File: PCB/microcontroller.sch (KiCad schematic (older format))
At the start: 6 parts, among them U1 DEV_KIT_EK-TM4C123GXL, U301 MC14504B

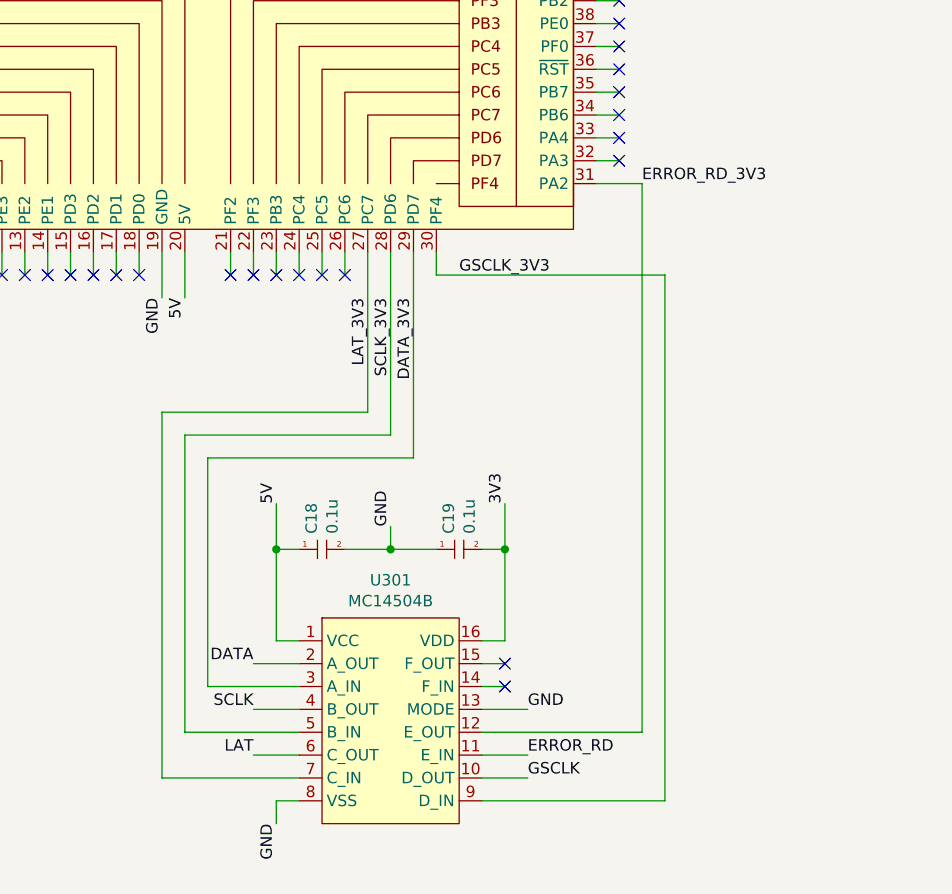
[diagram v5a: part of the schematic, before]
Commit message: V1.0 Ready for Review
Added compatability with the 430BOOST-C55AUDIO1 booster pack.
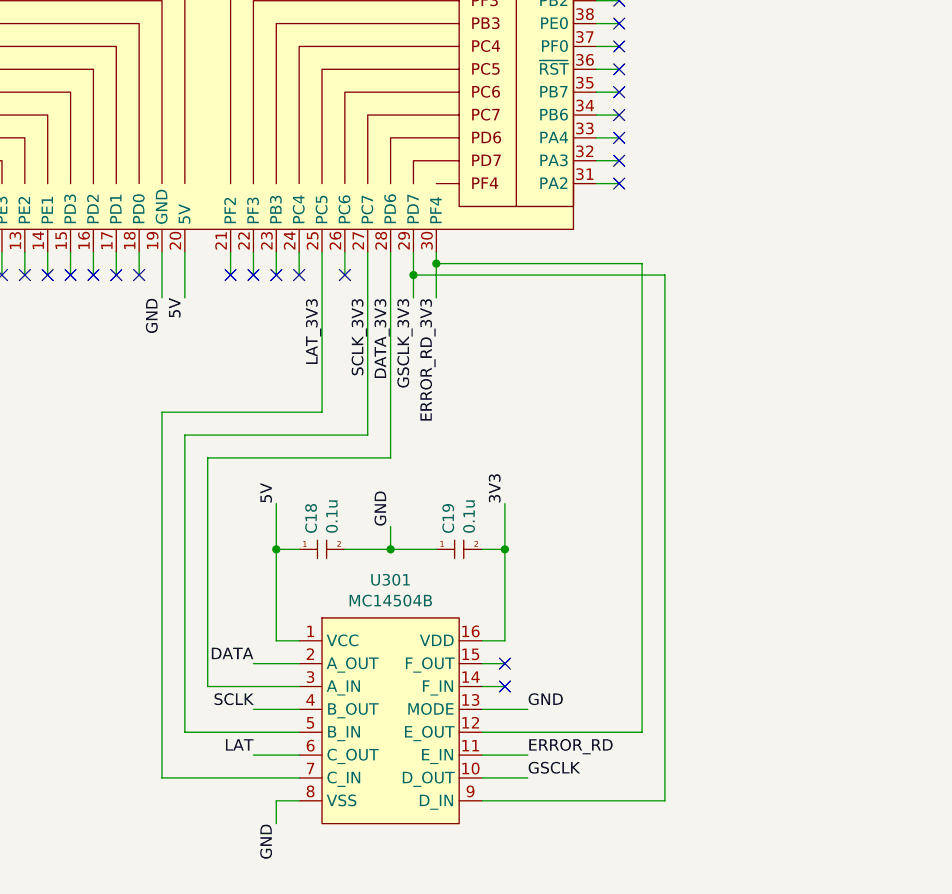
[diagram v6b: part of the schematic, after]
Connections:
- net DATA_3V3: now also U1.28 (PD6); no longer U1.29 (PD7)
- net ERROR_RD_3V3: now also U1.30 (PF4); no longer U1.31 (PA2)
- net GSCLK_3V3: now also U1.29 (PD7); no longer U1.30 (PF4)
- net LAT_3V3: now also U1.25 (PC5); no longer U1.27 (PC7)
- net SCLK_3V3: now also U1.27 (PC7); no longer U1.28 (PD6)
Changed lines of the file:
@@
 Sheet 3 20
 Title "Christmas Tree Disco"
-Date "2017-08-01"
+Date "2017-08-08"
 Rev "01"
 Comp "www.GitHub.com/Cryochasm"
@@
 Wire Wire Line
 	6700 5400 7400 5400
-Wire Wire Line
-	7200 3000 7400 3000
-Wire Wire Line
-	7400 3000 7400 5400
 NoConn ~ 6800 5100
 NoConn ~ 6800 5200
 Wire Wire Line
-	6500 3300 6500 3400
-Wire Wire Line
-	6500 3400 7500 3400
+	6500 3300 6500 3500
 Wire Wire Line
 	7500 3400 7500 5700
@@
 	5500 5200 5500 4200
 Wire Wire Line
-	5500 4200 6400 4200
-Wire Wire Line
-	6400 4200 6400 3300
-Wire Wire Line
 	5900 5400 5400 5400
 Wire Wire Line
 	5400 5400 5400 4100
 Wire Wire Line
-	5400 4100 6300 4100
-Wire Wire Line
-	6300 4100 6300 3300
-Wire Wire Line
 	5900 5600 5300 5600
 Wire Wire Line
 	5300 5600 5300 4000
-Wire Wire Line
-	5300 4000 6200 4000
-Wire Wire Line
-	6200 4000 6200 3300
 Wire Wire Line
 	3800 2200 3700 2200
@@
 	5900 3300 5900 3400
 Wire Wire Line
-	6000 3300 6000 3400
+	6000 3300 6000 4000
 Wire Wire Line
 	6100 3300 6100 3400
@@
 NoConn ~ 5800 3400
 NoConn ~ 5900 3400
-NoConn ~ 6000 3400
+NoConn ~ 7300 3000
 NoConn ~ 6100 3400
 Wire Wire Line
@@
 Text Label 6300 4500 1    50   ~ 0
 GND
-Text Label 6600 3400 0    50   ~ 0
+Text Label 6400 3500 3    50   ~ 0
 GSCLK_3V3
-Text Label 7400 3000 0    50   ~ 0
+Text Label 6500 3500 3    50   ~ 0
 ERROR_RD_3V3
-Text Label 6400 3500 3    50   ~ 0
+Text Label 6300 3500 3    50   ~ 0
 DATA_3V3
-Text Label 6300 3500 3    50   ~ 0
+Text Label 6200 3500 3    50   ~ 0
 SCLK_3V3
-Text Label 6200 3500 3    50   ~ 0
+Text Label 6000 3500 3    50   ~ 0
 LAT_3V3
 $Comp
@@
 	1    0    0    -1
 $EndComp
+Wire Wire Line
+	6400 3300 6400 3500
+Wire Wire Line
+	6400 3400 7500 3400
+Connection ~ 6400 3400
+Wire Wire Line
+	6500 3350 7400 3350
+Connection ~ 6500 3350
+Wire Wire Line
+	7400 3350 7400 5400
+Wire Wire Line
+	6300 3300 6300 4200
+Wire Wire Line
+	6300 4200 5500 4200
+Wire Wire Line
+	6200 3300 6200 4100
+Wire Wire Line
+	6200 4100 5400 4100
+Wire Wire Line
+	6000 4000 5300 4000
+Wire Wire Line
+	7300 3000 7200 3000
 $EndSCHEMATC

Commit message: Gerber Updates
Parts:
- renumbered H301 to H2, H302 to H4, U301 to U4
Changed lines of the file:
@@
 Title "Christmas Tree Disco"
 Date "2017-08-08"
-Rev "01"
+Rev "V1.0"
 Comp "www.GitHub.com/Cryochasm"
 Comment1 ""
@@
 GND
 $Comp
-L Generic H301
+L Generic H2
 U 1 1 5984BC75
 P 8500 1700
-F 0 "H301" H 8628 1746 50  0000 L CNN
+F 0 "H2" H 8628 1746 50  0000 L CNN
 F 1 "2x10 HEADER" H 8628 1655 50  0000 L CNN
 F 2 "local:2x10_header_3d" H 8500 1500 50  0001 C CNN
@@
 $EndComp
 $Comp
-L Generic H302
+L Generic H4
 U 1 1 5984BD4E
 P 8500 2000
-F 0 "H302" H 8628 2046 50  0000 L CNN
+F 0 "H4" H 8628 2046 50  0000 L CNN
 F 1 "2x10 HEADER" H 8628 1955 50  0000 L CNN
 F 2 "local:2x10_header_3d" H 8500 1800 50  0001 C CNN
@@
 $EndComp
 $Comp
-L MC14504B U301
+L MC14504B U4
 U 1 1 5984BDBB
 P 6300 5300
-F 0 "U301" H 6300 5865 50  0000 C CNN
+F 0 "U4" H 6300 5865 50  0000 C CNN
 F 1 "MC14504B" H 6300 5774 50  0000 C CNN
 F 2 "local:SOIC-16" H 6200 5800 50  0001 C CNN
